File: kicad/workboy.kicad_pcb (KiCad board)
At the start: 2 copper layers, 152 x 106.1 mm, 131 parts, among them J1 GB-LINK, J2 ISP-2x3, J3 USB-C-16P, SW1 TACT_6mm, SW10 TACT_6mm, SW11 TACT_6mm, SW12 TACT_6mm, SW13 TACT_6mm, SW14 TACT_6mm, SW15 TACT_6mm, SW16 TACT_6mm, SW17 TACT_6mm, SW18 TACT_6mm, SW19 TACT_6mm, SW2 TACT_6mm, SW20 TACT_6mm, SW21 TACT_6mm, SW22 TACT_6mm, SW23 TACT_6mm, SW24 TACT_6mm, SW25 TACT_6mm, SW26 TACT_6mm, SW27 TACT_6mm, SW28 TACT_6mm, SW29 TACT_6mm, SW3 TACT_6mm, SW30 TACT_6mm, SW31 TACT_6mm, SW32 TACT_6mm, SW33 TACT_6mm, SW34 TACT_6mm, SW35 TACT_6mm, SW36 TACT_6mm, SW37 TACT_6mm, SW38 TACT_6mm, SW39 TACT_6mm, SW4 TACT_6mm, SW40 TACT_6mm, SW41 TACT_6mm, SW42 TACT_6mm, SW43 TACT_6mm, SW44 TACT_6mm, SW45 TACT_6mm, SW46 TACT_6mm, SW47 TACT_6mm, SW48 TACT_6mm, SW49 TACT_6mm, SW5 TACT_6mm, SW50 TACT_6mm, SW51 TACT_6mm, SW52 TACT_6mm, SW53 TACT_6mm, SW6 TACT_6mm, SW7 TACT_6mm, SW8 TACT_6mm, SW9 TACT_6mm, U1 ATmega328P-AU

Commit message: feat(pcb): add four M2.5 mounting holes and re-export
The board had none, while BUILD_PLAN promised 4x M2.5 and the case drilled four
standoffs against hole positions that described a board that does not exist.

H1-H4 are plain NPTH MountingHole_2.7mm_M2.5, 4.0 mm inset from the Edge.Cuts
centreline at each corner, symmetric about the board centre (150.0, 89.0625):

  H1 ( 78.000,  40.000)   H2 (222.000,  40.000)
  H3 ( 78.000, 138.125)   H4 (222.000, 138.125)     spacing 144.000 x 98.125 mm

Positions were chosen by scanning clearance against every pad, track, via and part
body rather than by eye. Insets of 4.0-5.5 mm all clear; 6.0 mm fails because the
top-right hole starts fouling SW12. 4.0 mm maximises clearance at that tightest
corner - H2 sits 4.607 mm from copper and 4.475 mm from SW12's body, so a 5 mm
case post keeps 1.98 mm of margin. The right-hand border is only 2.05 mm wide
(J3 runs close to it), so the corners are the only viable positions and there is
no room for a centre boss.

Verified after the change:

- DRC --severity-all --exit-code-violations: 0 violations, 0 unconnected, 0
  footprint errors, exit 0
- Edge_Cuts and F_Cu gerbers differ ONLY in the version string and timestamp, so
  the outline is untouched and the holes add no copper - they really are NPTH
- workboy.drl gains T6C2.700 with exactly 4 hits at those coordinates, tagged
  NonPlated/NPTH/ComponentDrill
- CPL still lists 131 parts and the BOM is byte-unchanged, because the holes are
  marked exclude-from-BOM and exclude-from-position-files

H1-H4 are also added to generate_workboy_netlist.py as netless components. They
were placed directly in the PCB, and KiCad deletes footprints absent from an
imported netlist - without this, the next netlist import would silently remove
them. Component count now matches the board at 135.

All artefacts re-exported from the modified board: gerbers, drill, position/CPL,
STEP and the gerber zip. Note the exports move from KiCad 10.0.3 to 10.0.5, which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
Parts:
- added H1: MountingHole_2.7mm_M2.5, MountingHole_2.7mm_M2.5, F.Cu at (78.0, 40.0)
- added H2: MountingHole_2.7mm_M2.5, MountingHole_2.7mm_M2.5, F.Cu at (222.0, 40.0)
- added H3: MountingHole_2.7mm_M2.5, MountingHole_2.7mm_M2.5, F.Cu at (78.0, 138.1)
- added H4: MountingHole_2.7mm_M2.5, MountingHole_2.7mm_M2.5, F.Cu at (222.0, 138.1)

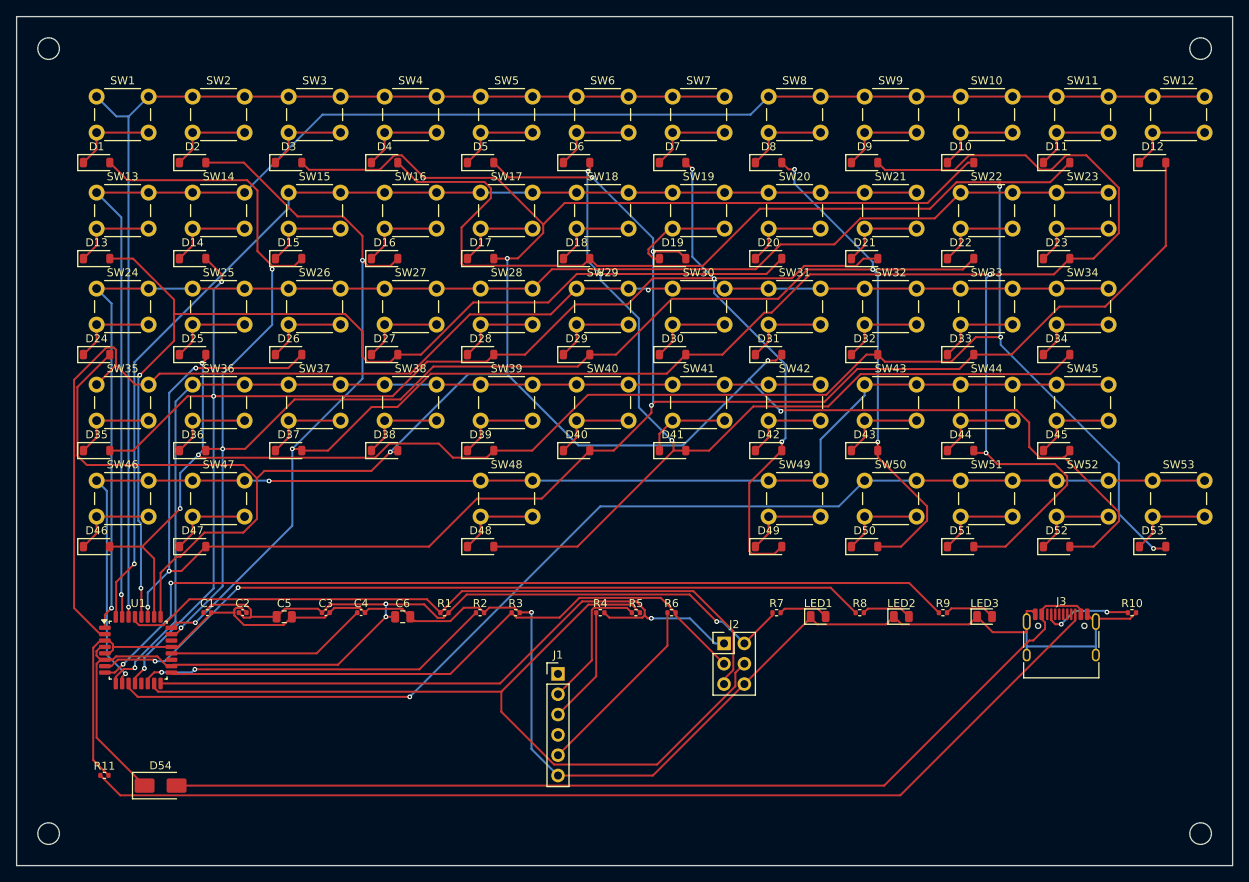
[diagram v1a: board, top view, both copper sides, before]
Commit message: feat(pcb): move J3 USB-C to the right board edge and re-route
J3 sat 16.07 mm inside the outline, so no USB-C plug could reach it - a case
would have needed a 16 mm channel through the wall. It is now flush with the
right edge, rotated 90 so the mating face points outward, body front on the
outline and the courtyard overhanging by 0.525 mm as an edge connector should.

Moving it exposed a second, latent problem. gen_pcb.py placed support parts with
a row-wrapping flow, and the ["J3","R10","R11","D54"] group happened to straddle
a wrap - stranding the CC2 pulldown and the VBUS Schottky ~130 mm away on the far
side of the board and dragging the unfused power input across the whole PCB. That
was an artifact of the layout algorithm, not a decision. The cluster is now placed
explicitly beside J3.

  J3 -> right edge     16.07 mm inland  ->  -0.525 mm (overhangs)
  R11 -> J3            138.31 mm        ->  9.37 mm
  D54 -> J3            131.51 mm        ->  12.35 mm
  total VBUS copper    ~112 mm          ->  13.7 mm

The board outline is now PINNED in gen_pcb.py rather than derived from the
bounding box of whatever is placed. Deriving it meant moving any single part could
silently resize the board, and the size is load-bearing for the case, the mounting
holes and the quote. Placement is asserted to fit inside instead, and the script
refuses to write a board that overflows.

Verified: DRC 0 violations, 0 unconnected, 0 footprint errors. The Edge_Cuts
gerber differs by a single nanometre (Y-142124999 -> Y-142125000, the exact pinned
constant replacing a computed one), and the CPL differs only in the four moved
parts - everything else is untouched. workboy.net and the BOM are unchanged, since
placement does not affect connectivity. Case regenerates identically and now cuts
its J3 port and J1 slot from the real connector coordinates instead of hard-coded
ones. Full CI passes 4/4.

Two traps worth not rediscovering, recorded in PCB_README.md:

- gen_pcb.py ordering is load-be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
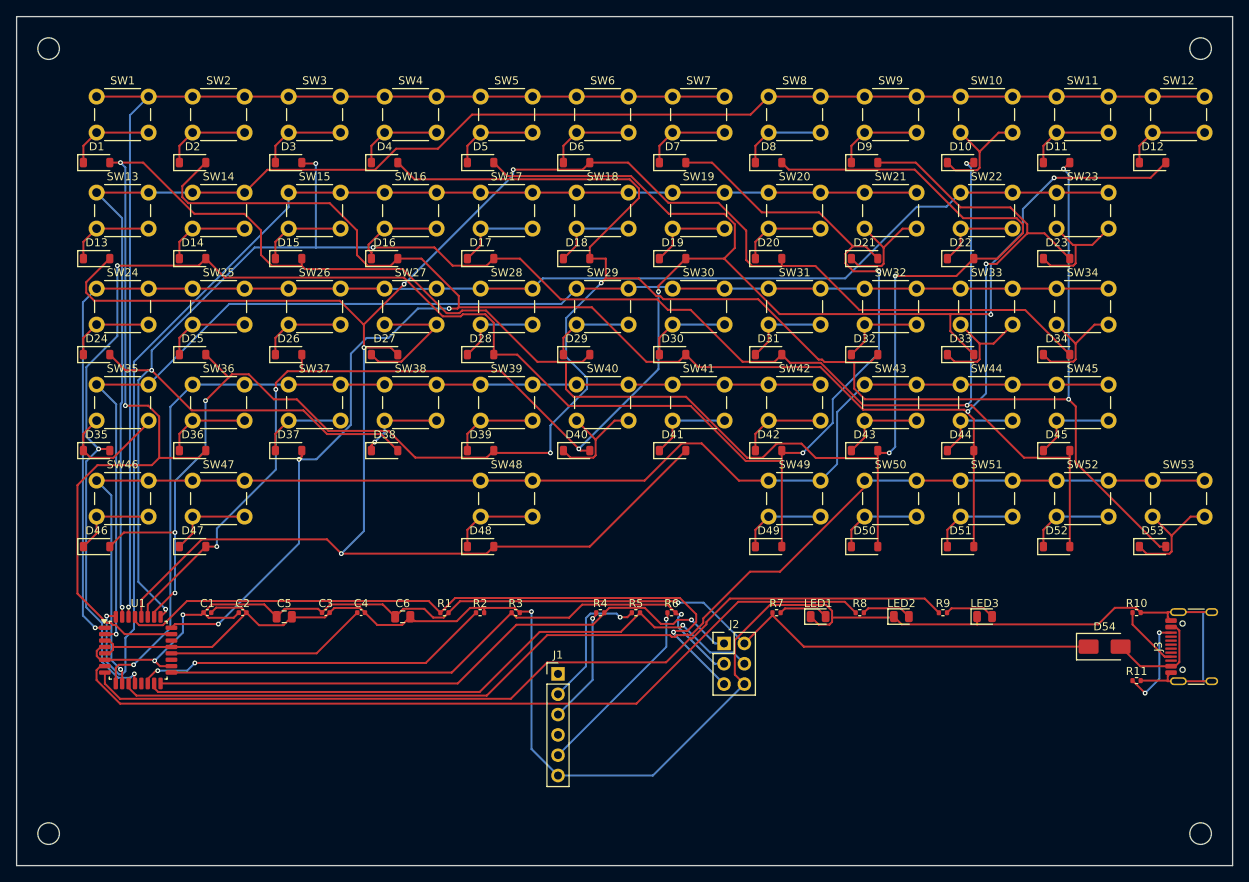
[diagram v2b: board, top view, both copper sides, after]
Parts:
- H1, H2, H3, H4: value MountingHole_2.7mm_M2.5 -> MountingHole_M2.5
- moved R11 129.6 mm to (214.0, 119.0)
- moved D54 119.3 mm to (210.0, 114.8)
- moved J3 17.8 mm to (222.3, 114.8), turned to 90 degrees
- moved R10 0.58 mm to (214.0, 110.5)
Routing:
- net USB_CC2: track 132.7 -> 12.0 mm, vias 0 -> 2
- net VBUS: track 125.1 -> 13.7 mm
- net COL2: track 323.5 -> 265.3 mm, vias 4 -> 6
- net COL0: track 251.9 -> 295.5 mm, vias 6 -> 4
- net COL1: track 295.0 -> 257.0 mm
- net MCU_MOSI: track 108.2 -> 81.5 mm, vias 0 -> 1
- net COL3: track 311.2 -> 289.6 mm, vias 6 -> 7
- net COL4: track 249.3 -> 232.6 mm
- net ROW2: track 140.5 -> 156.8 mm
- net GND: track 201.4 -> 213.8 mm
- net ROW4: track 176.3 -> 165.3 mm
- net COL6: track 224.7 -> 234.9 mm, vias 6 -> 5
- net KEY27: track 10.9 -> 17.1 mm
- net MCU_MISO: track 82.7 -> 76.6 mm
- net COL5: track 260.0 -> 265.7 mm, vias 5 -> 4
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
